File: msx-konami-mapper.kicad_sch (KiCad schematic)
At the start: 5 parts, among them SW1 High/Low, U1 SST39SF040, U3 74LS670

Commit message: Yes, I need another 670
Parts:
- added U4: 74LS670, Package_DIP:DIP-16_W7.62mm_Socket_LongPads, symbol 74xx:74LS670
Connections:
- net +5V: now also U4.16 (VCC)
- net GND: now also U4.8 (GND)
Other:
- moved on the sheet: JP1, SW1, U1, U3

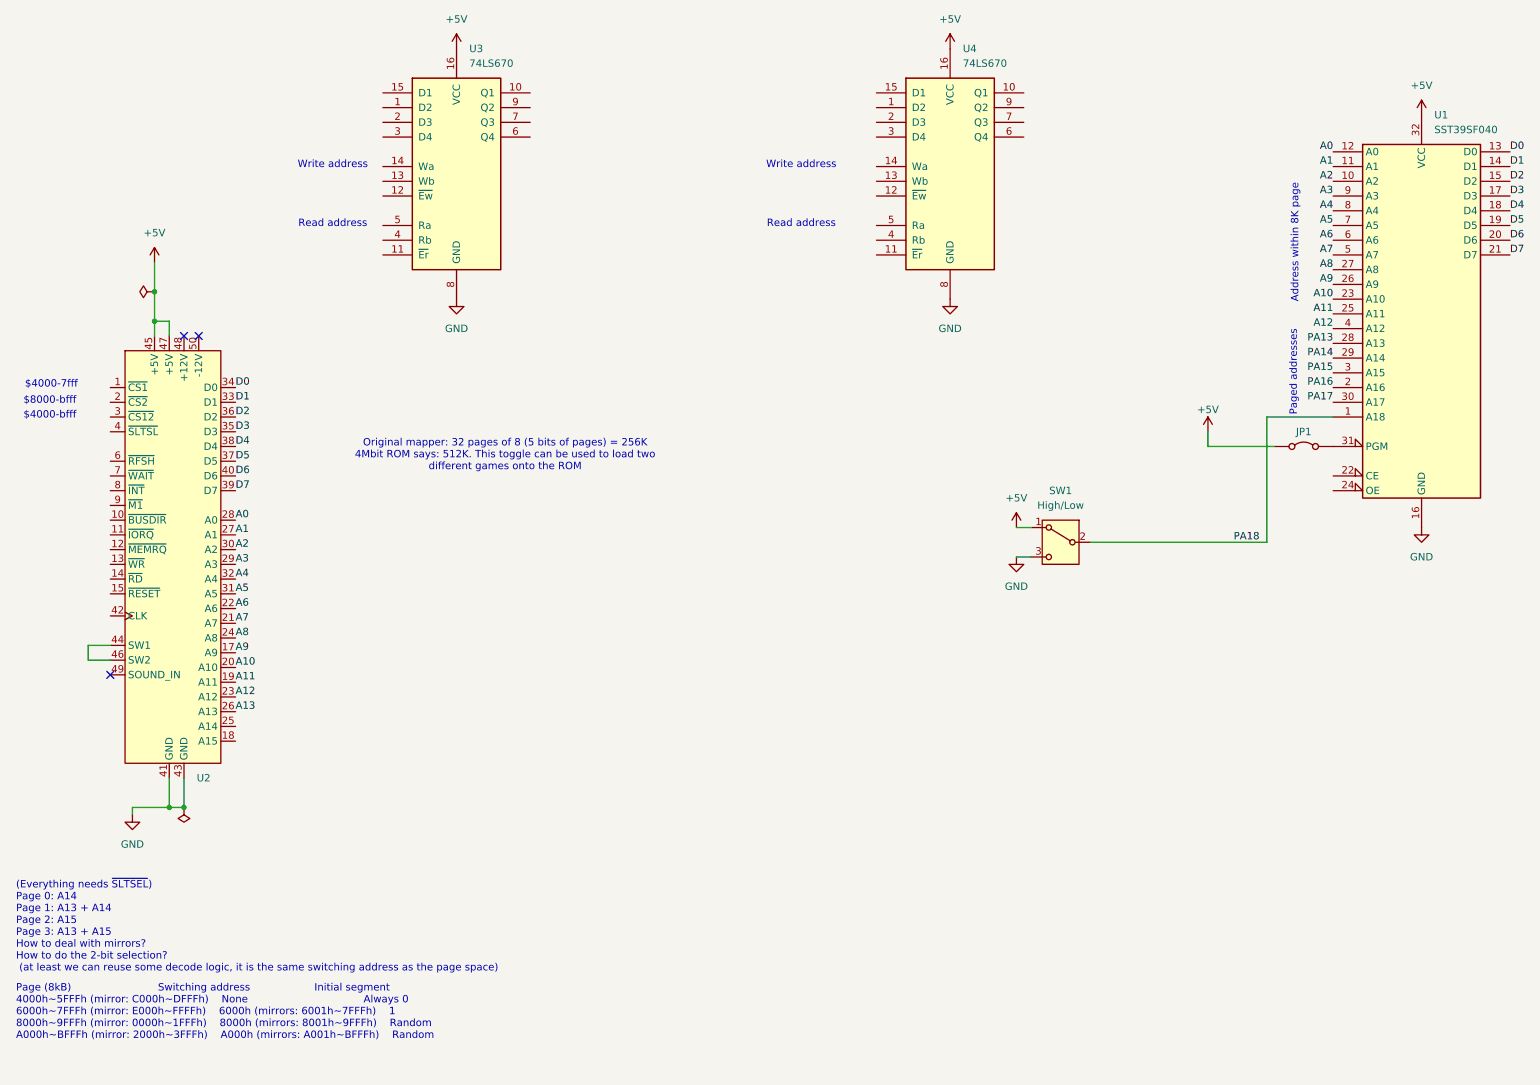
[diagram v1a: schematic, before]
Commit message: Driving 8 bits of pages
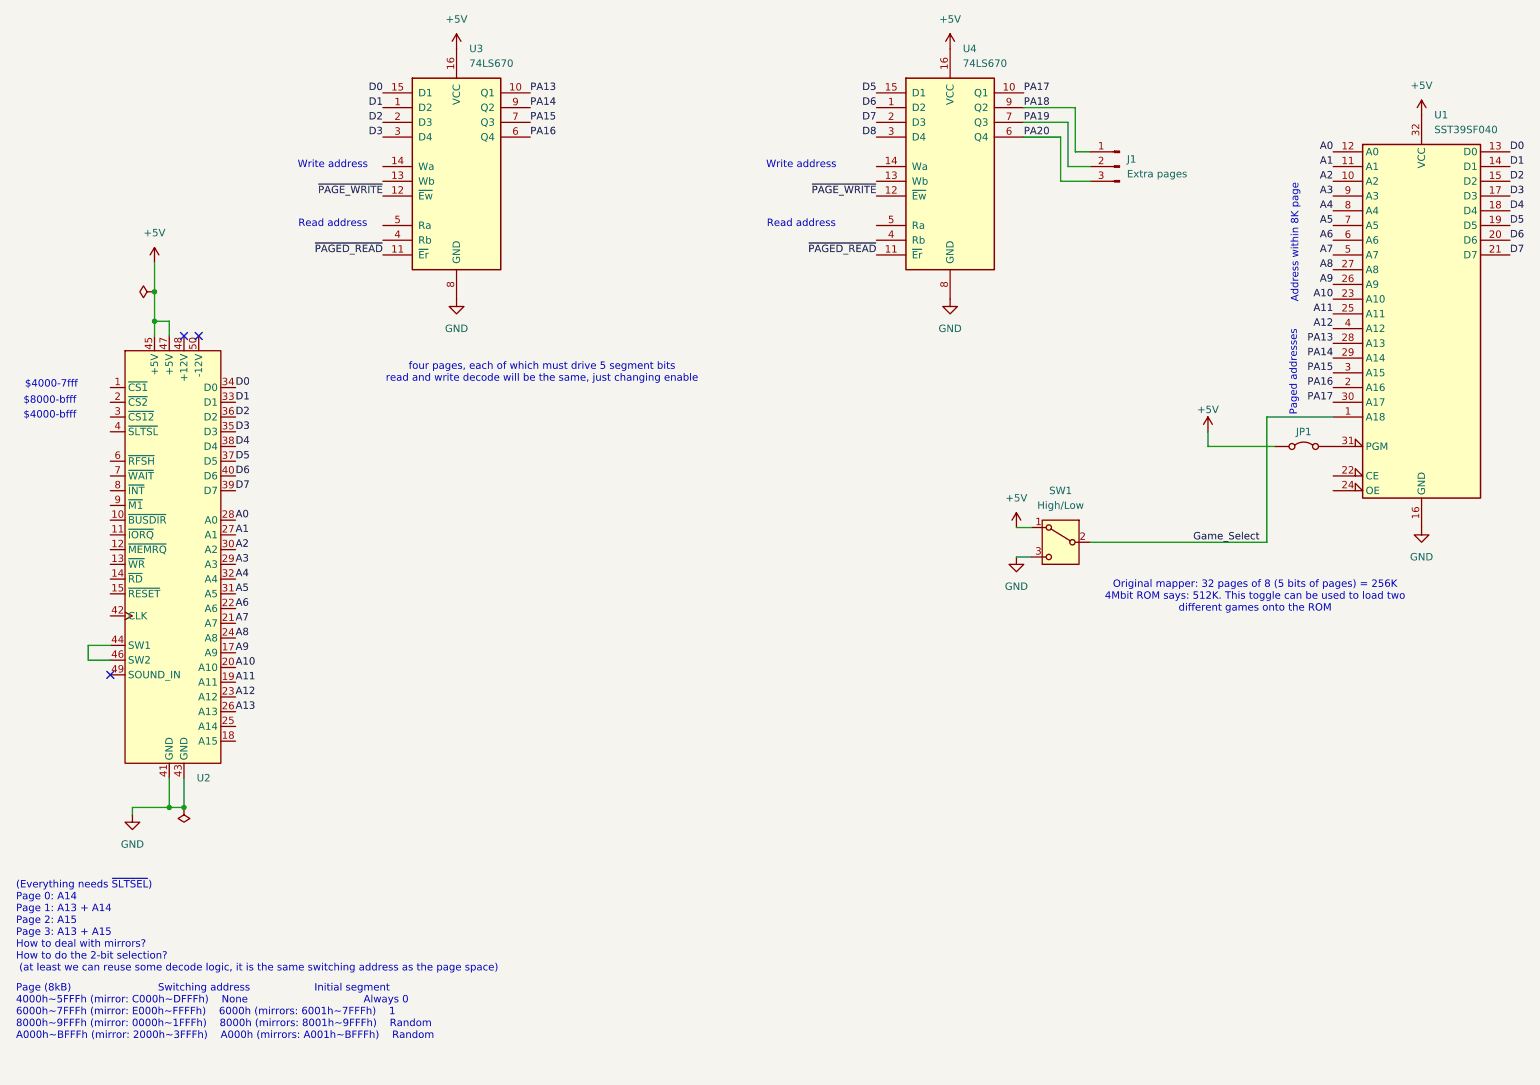
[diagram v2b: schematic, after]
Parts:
- added J1: Extra pages, Connector_PinHeader_2.54mm:PinHeader_1x03_P2.54mm_Vertical, symbol Connector:Conn_01x03_Pin
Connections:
- net D0: now also U3.15 (D1)
- net D1: now also U3.1 (D2)
- net D2: now also U3.2 (D3)
- net D3: now also U3.3 (D4)
- net D5: now also U4.15 (D1)
- net D6: now also U4.1 (D2)
- net D7: now also U4.2 (D3)
- net PA13: now also U3.10 (Q1)
- net PA14: now also U3.9 (Q2)
- net PA15: now also U3.7 (Q3)
- net PA16: now also U3.6 (Q4)
- net PA17: now also U4.10 (Q1)
- net PA18: now also U4.9 (Q2), J1.1 (Pin_1); no longer SW1.2 (B), U1.1 (A18)
- net ~{PAGED_READ}: now reaches U4.11 (~{Er})
- net ~{PAGED_READ}: now also U3.11 (~{Er})
- net ~{PAGE_WRITE}: now reaches U4.12 (~{Ew})
- net ~{PAGE_WRITE}: now also U3.12 (~{Ew})
- net D8: now reaches U4.3 (D4)
- net PA20: now reaches U4.6 (Q4)
- net PA20: now also J1.3 (Pin_3)
- net PA19: now reaches U4.7 (Q3)
- net PA19: now also J1.2 (Pin_2)
- new net Game_Select: SW1.2 (B), U1.1 (A18)
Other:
- note added: "four pages, each of which must drive 5 segment bits read and write decode will be the same, just changing enable"

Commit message: Undoing bad work
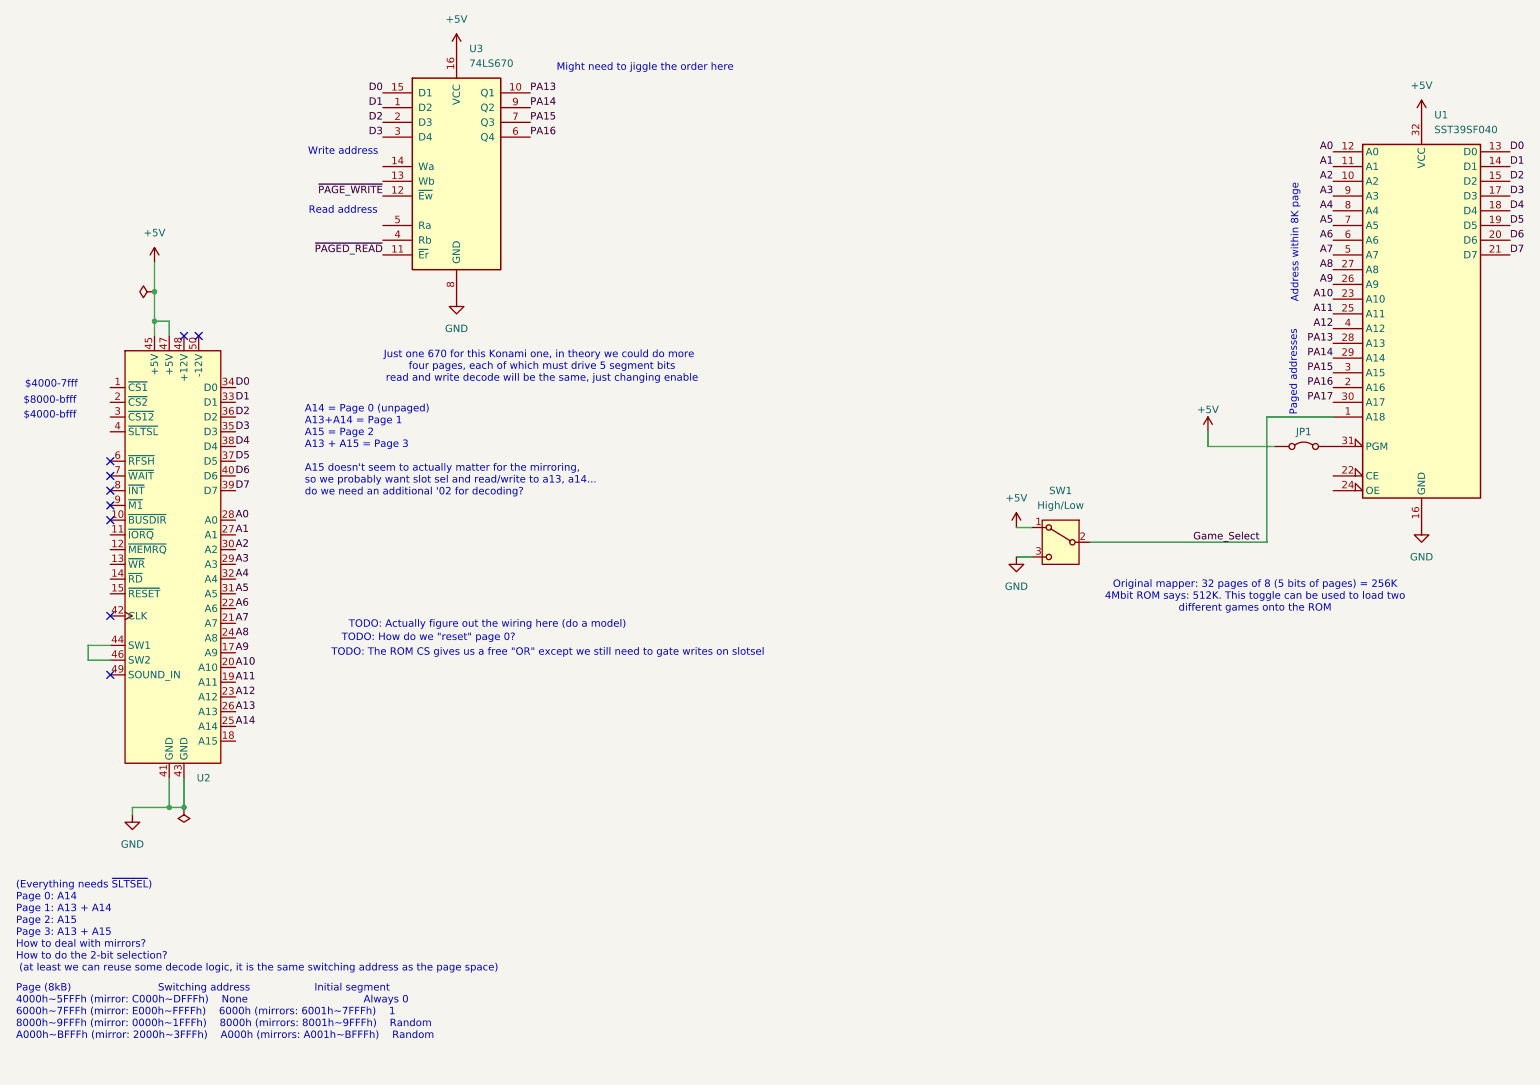
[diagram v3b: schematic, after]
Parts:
- removed J1: Extra pages, Connector_PinHeader_2.54mm:PinHeader_1x03_P2.54mm_Vertical, symbol Connector:Conn_01x03_Pin
- removed U4: 74LS670, Package_DIP:DIP-16_W7.62mm_Socket_LongPads, symbol 74xx:74LS670
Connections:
- net A14: now reaches U2.25 (A14)
- no-connect marks 3 -> 9
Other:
- note added: "A14 = Page 0 (unpaged) A13+A14 = Page 1 A15 = Page 2 A13 + A15 = Page 3 A15 doesn't seem to actually matter for the mirroring, so we probably want slot sel and read/write to a13, a14... do we need an additional '02 for decoding?"
- note added: "Just one 670 for this Konami one, in theory we could do more"
- note added: "Might need to jiggle the order here"
- note added: "TODO: Actually figure out the wiring here (do a model)"
- note added: "TODO: How do we "reset" page 0?"
- note added: "TODO: The ROM CS gives us a free "OR" except we still need to gate writes on slotsel"

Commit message: I think this works
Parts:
- removed SW1: High/Low, Connector_PinHeader_2.54mm:PinHeader_1x03_P2.54mm_Vertical, symbol Switch:SW_SPDT
- added C1, C2, C3: 0.1µF, Capacitor_THT:C_Disc_D3.8mm_W2.6mm_P2.50mm, symbol Device:C_Small
- added R1, R2: 10kΩ, Resistor_THT:R_Axial_DIN0207_L6.3mm_D2.5mm_P10.16mm_Horizontal, symbol Device:R_Small_US
- added SW1: Bonus Games, Button_Switch_THT:SW_DIP_SPSTx02_Slide_9.78x7.26mm_W7.62mm_P2.54mm, symbol Switch:SW_DIP_x02
- added U4: 74LS02, Package_DIP:DIP-14_W7.62mm_Socket_LongPads, symbol 74xx:74LS02
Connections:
- net Game_Select is gone; now on net +5V: U1.1 (A18)
- net +5V: now also C1.1, C2.1, C3.1, R1.1, R2.1, R2.2, SW1.3, U4.14 (VCC)
- net A13: now also U3.13 (Wb), U3.4 (Rb), U4.9
- net D0: now also U3.3 (D4); no longer U3.15 (D1)
- net D1: now also U3.2 (D3); no longer U3.1 (D2)
- net D2: now also U3.1 (D2); no longer U3.2 (D3)
- net D3: now also U3.15 (D1); no longer U3.3 (D4)
- net GND: now also C1.2, C2.2, C3.2, SW1.1, SW1.2, U4.11, U4.12, U4.7 (GND)
- net PA13: now also U3.6 (Q4); no longer U3.10 (Q1)
- net PA14: now also U3.7 (Q3); no longer U3.9 (Q2)
- net PA15: now also U3.9 (Q2); no longer U3.7 (Q3)
- net PA16: now also U3.10 (Q1); no longer U3.6 (Q4)
- net ~{PAGED_READ}: now also U4.10
- net ~{PAGE_WRITE}: now also U4.4
- net ~{WR}: now reaches U2.13 (~{WR})
- net ~{WR}: now also U4.2
- net A15: now reaches U2.18 (A15)
- net A15: now also U3.14 (Wa), U3.5 (Ra), U4.8
- net ~{SLTSL}: now reaches U2.4 (~{SLTSL})
- net ~{SLTSL}: now also U1.22 (CE), U4.3
- net ~{RD}: now reaches U1.24 (OE)
- net PA17: no longer names the net of U1.30 (A17)
- net PA17: now also R1.2, SW1.4
- new net: U4.1, U4.5, U4.6
- no-connect marks 9 -> 17
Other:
- note added: "I suspect the "initial segment 1" for page 1 is set by software"
- note added: "Just one 670 for this Konami one (128k games), in theory we could do more"
- note removed: "Just one 670 for this Konami one, in theory we could do more"
- note removed: "Might need to jiggle the order here"
- note removed: "Original mapper: 32 pages of 8 (5 bits of pages) = 256K 4Mbit ROM says: 512K. This toggle can be used to load two different games onto the ROM"
- note removed: "TODO: Actually figure out the wiring here (do a model)"
- note removed: "TODO: How do we "reset" page 0?"
- note removed: "TODO: The ROM CS gives us a free "OR" except we still need to gate writes on slotsel"
- note removed: "four pages, each of which must drive 5 segment bits read and write decode will be the same, just changing enable"
- moved on the sheet: U3

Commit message: Routed
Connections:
- net +5V: no longer R2.2, SW1.3, U1.1 (A18)
- net ~{RD}: now also U2.14 (~{RD})
- new net: R2.2, SW1.3, U1.1 (A18)
- no-connect marks 17 -> 16
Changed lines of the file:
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@@
-	)
-	(junction
-		(at 238.76 90.17)
-		(diameter 0)
-		(color 0 0 0 0)
 	)
 	(junction
@@
 		(at 38.1 97.79)
 	)
-	(no_connect
-		(at 38.1 113.03)
-	)
 	(wire
 		(pts
@@
 	(wire
 		(pts
-			(xy 238.76 85.09) (xy 238.76 90.17)
+			(xy 238.76 85.09) (xy 238.76 102.87)
 		)
 		(stroke
@@
 		(pts
 			(xy 48.26 71.12) (xy 48.26 68.58)
-		)
-		(stroke
-			(width 0)
-			(type default)
-		)
-	)
-	(wire
-		(pts
-			(xy 238.76 90.17) (xy 238.76 102.87)
 		)
 		(stroke
@@
 		(fields_autoplaced yes)
 		(effects
+			(font
+				(size 1.27 1.27)
+			)
+			(justify right bottom)
+		)
+	)
+	(label "~{RD}"
+		(at 38.1 113.03 180)
+		(fields_autoplaced yes)
+		(effects

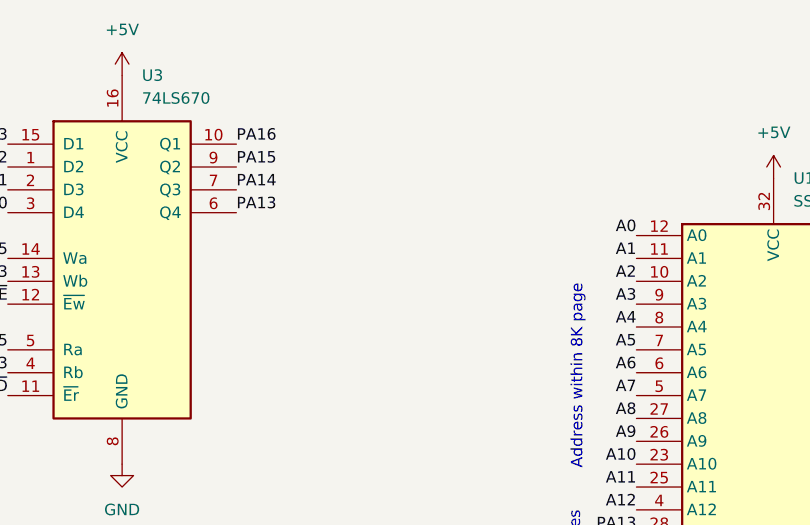
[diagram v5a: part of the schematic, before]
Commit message: Pull-downs for '670 output
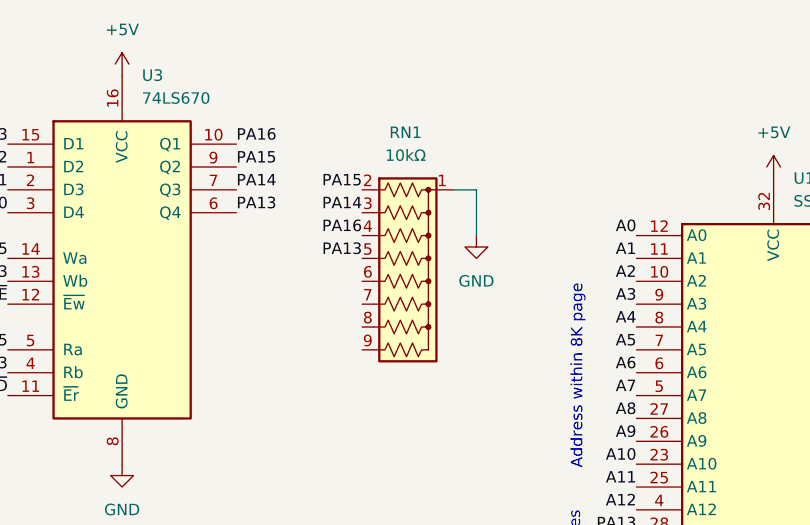
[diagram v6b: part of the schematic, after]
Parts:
- added RN1: 10kΩ, Resistor_THT:R_Array_SIP9, symbol Device:R_Network08_US
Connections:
- net GND: now also RN1.1 (common)
- net PA13: now also RN1.5 (R4)
- net PA14: now also RN1.3 (R2)
- net PA15: now also RN1.2 (R1)
- net PA16: now also RN1.4 (R3)
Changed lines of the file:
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@@
 	(wire
 		(pts
+			(xy 231.14 34.29) (xy 228.6 34.29)
+		)
+		(stroke
+			(width 0)
+			(type default)
+		)
+	)
+	(wire
+		(pts
 			(xy 238.76 102.87) (xy 212.09 102.87)
 		)
@@
 	(wire
 		(pts
+			(xy 231.14 39.37) (xy 231.14 34.29)
+		)
+		(stroke
+			(width 0)
+			(type default)
+		)
+	)
+	(wire
+		(pts
 			(xy 34.29 127) (xy 38.1 127)
 		)
@@
 		)
 	)
+	(label "PA16"
+		(at 218.44 39.37 180)
+		(fields_autoplaced yes)
+		(effects
+			(font
+				(size 1.27 1.27)
+			)
+			(justify right bottom)
+		)
+	)
 	(label "A0"
 		(at 248.92 39.37 180)
@@
 		)
 	)
+	(label "PA15"
+		(at 218.44 34.29 180)
+		(fields_autoplaced yes)
+		(effects
+			(font
+				(size 1.27 1.27)
+			)
+			(justify right bottom)
+		)
+	)
 	(label "A0"
 		(at 59.69 102.87 0)
@@
 		)
 	)
+	(label "PA13"
+		(at 218.44 41.91 180)
+		(fields_autoplaced yes)
+		(effects
+			(font
+				(size 1.27 1.27)
+			)
+			(justify right bottom)
+		)
+	)
 	(label "D3"
 		(at 279.4 46.99 0)
@@
 		)
 	)
+	(label "PA14"
+		(at 218.44 36.83 180)
+		(fields_autoplaced yes)
+		(effects
+			(font
+				(size 1.27 1.27)
+			)
+			(justify right bottom)
+		)
+	)
 	(label "~{SLTSL}"
 		(at 38.1 87.63 180)
@@
 	)
 	(symbol
+		(lib_id "power:GND")
+		(at 231.14 39.37 0)
+		(unit 1)
+		(exclude_from_sim no)
+		(in_bom yes)
+		(on_board yes)
+		(dnp no)
+		(fields_autoplaced yes)
+		(property "Reference" "#PWR015"
+			(at 231.14 45.72 0)
+			(effects
+				(font
+					(size 1.27 1.27)
+				)
+				(hide yes)
+			)
+		)
+		(property "Value" "GND"
+			(at 231.14 44.45 0)
+			(effects
+				(font
+					(size 1.27 1.27)
+				)
+			)
+		)
+		(property "Footprint" ""
+			(at 231.14 39.37 0)
+			(effects
+				(font
+					(size 1.27 1.27)
+				)
+				(hide yes)
+			)
+		)
+		(property "Datasheet" ""
+			(at 231.14 39.37 0)
+			(effects
+				(font
+					(size 1.27 1.27)
+				)
+				(hide yes)
+			)
+		)
+		(property "Description" "Power symbol creates a global label with name \"GND\" , ground"
+			(at 231.14 39.37 0)
+			(effects
+				(font
+					(size 1.27 1.27)
+				)
+				(hide yes)
+			)
+		)
+		(pin "1"
+		)
+		(instances
+			(project ""
+				(path "/3ac3ee82-802b-4f0f-99fb-f88e392aa8f2"
+					(reference "#PWR015")
+					(unit 1)
+				)
+			)
+		)
+	)
+	(symbol
 		(lib_id "MSX:Cartridge")
 		(at 49.53 76.2 0)
@@
 					(unit 1)
 				)
+			)
+		)
+	)
+	(symbol
+		(lib_id "Device:R_Network08_US")
+		(at 223.52 44.45 270)
+		(unit 1)
+		(exclude_from_sim no)
+		(in_bom yes)
+		(on_board yes)
+		(dnp no)
+		(fields_autoplaced yes)
+		(property "Reference" "RN1"
+			(at 223.266 27.94 90)
+			(effects
+				(font
+					(size 1.27 1.27)
+				)
+			)
+		)
+		(property "Value" "10kΩ"
+			(at 223.266 30.48 90)
+			(effects
+				(font
+					(size 1.27 1.27)
+				)
+			)
+		)
+		(property "Footprint" "Resistor_THT:R_Array_SIP9"
+			(at 223.52 56.515 90)
+			(effects
+				(font
+					(size 1.27 1.27)
+				)
+				(hide yes)
+			)
+		)
+		(property "Datasheet" "http://www.vishay.com/docs/31509/csc.pdf"
+			(at 223.52 44.45 0)
+			(effects
+				(font
+					(size 1.27 1.27)
+				)
+				(hide yes)
+			)
+		)
+		(property "Description" "8 resistor network, star topology, bussed resistors, small US symbol"
+			(at 223.52 44.45 0)
+			(effects
+				(font
+					(size 1.27 1.27)
+				)
+				(hide yes)
+			)
+		)
+		(pin "3"
+		)
+		(pin "2"
+		)
+		(pin "1"
+		)
+		(pin "4"
+		)
+		(pin "5"
+		)
+		(pin "6"
+		)
+		(pin "7"
+		)
+		(pin "8"
+		)
+		(pin "9"
+		)
+		(instances
+			(project ""
+				(path "/3ac3ee82-802b-4f0f-99fb-f88e392aa8f2"
+					(reference "RN1")
+					(unit 1)
+				)
